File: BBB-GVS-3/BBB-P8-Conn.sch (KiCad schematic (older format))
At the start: 14 parts, among them J12 CONN_3, J13 CONN_3, J14 CONN_3, J15 CONN_3, J16 CONN_3, J17 CONN_3, J18 CONN_3, J19 CONN_3, J20 CONN_3, J21 CONN_3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

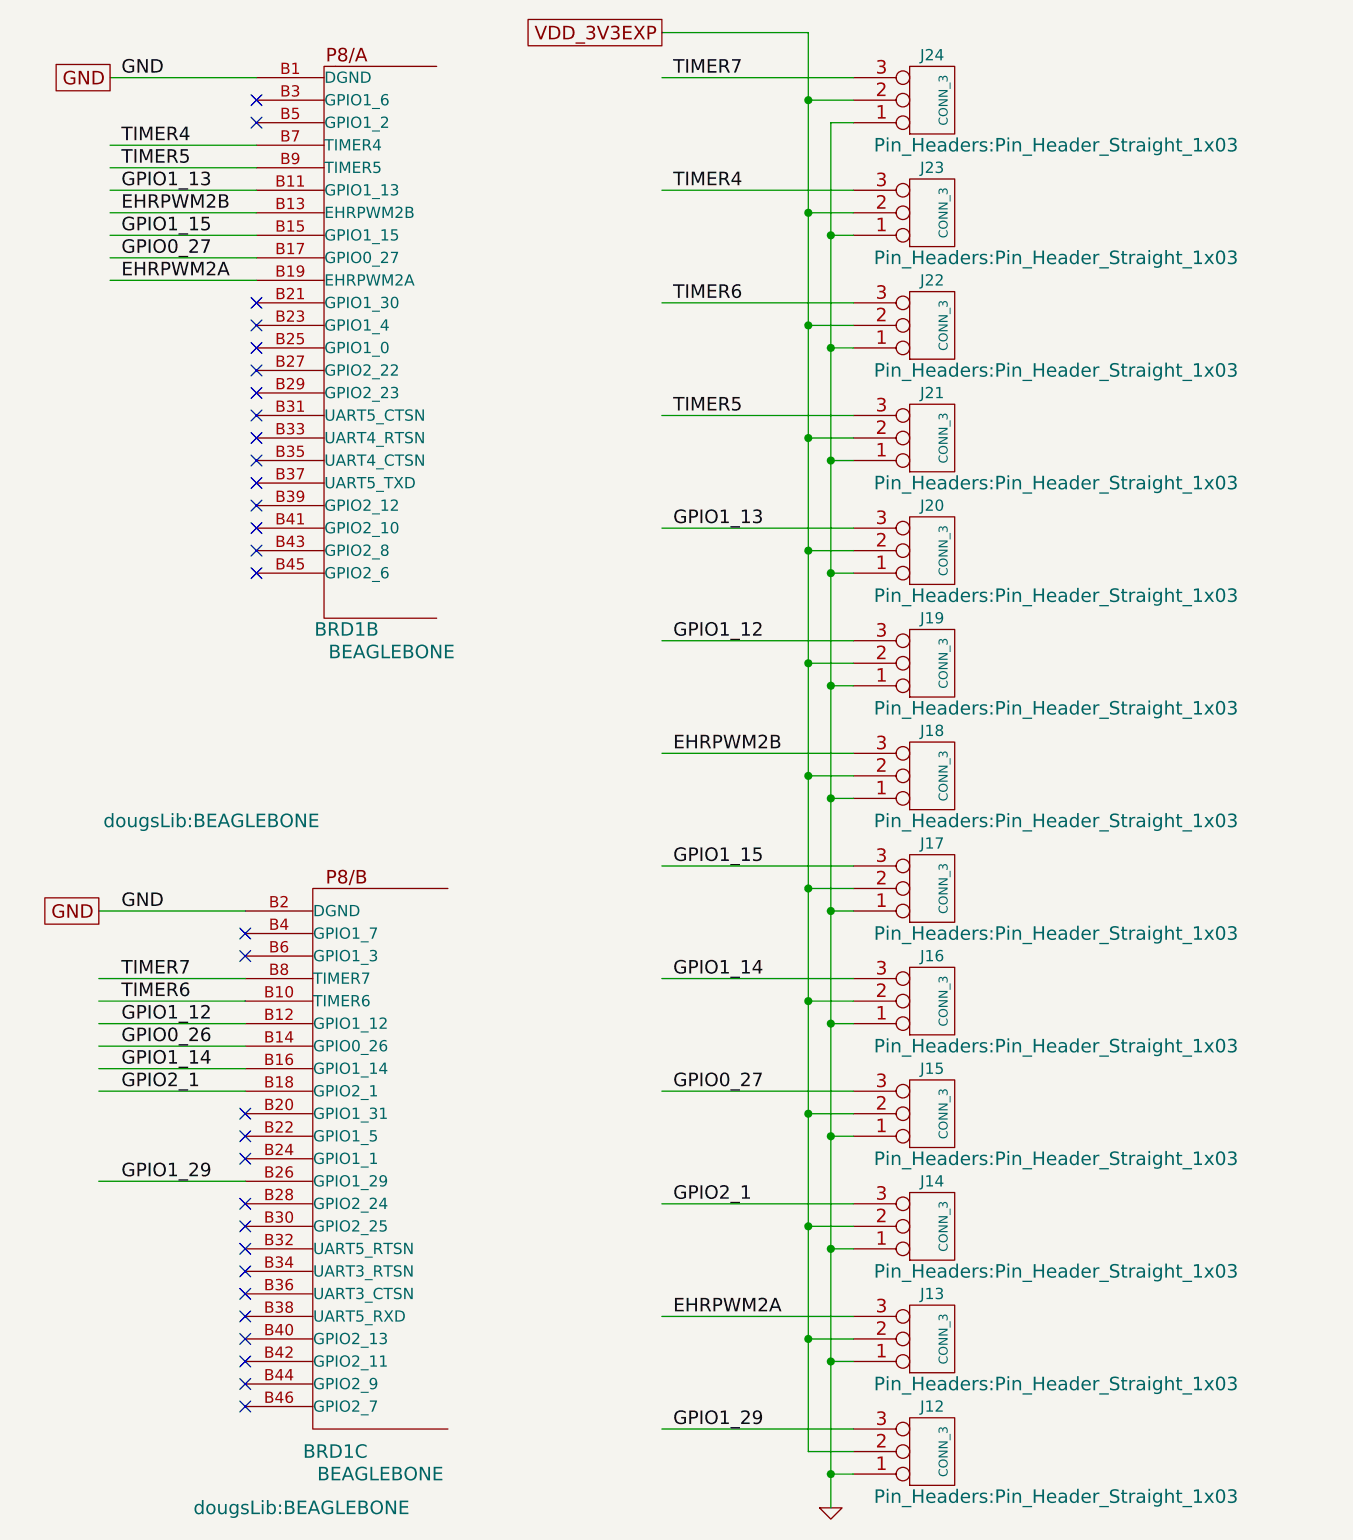
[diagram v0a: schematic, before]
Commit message: Changing GVS connector types
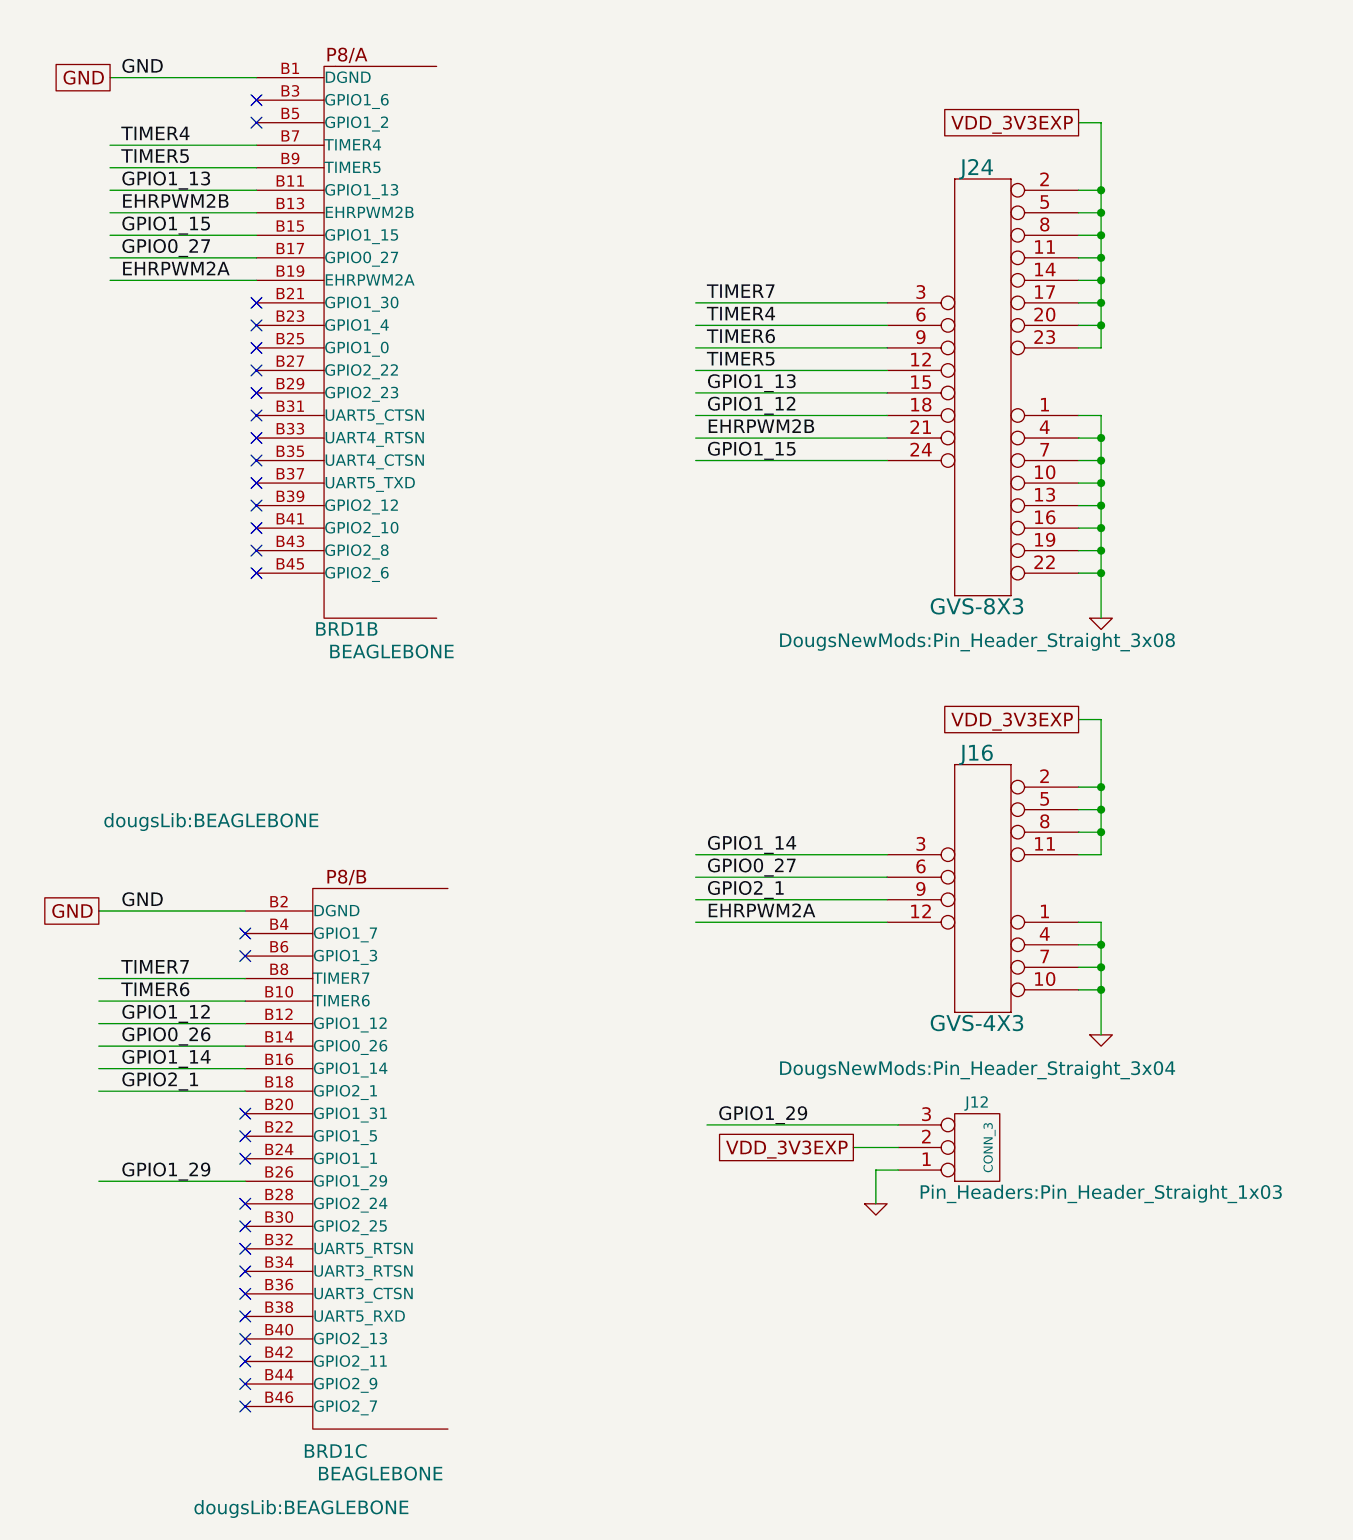
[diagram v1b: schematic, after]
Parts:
- removed J13, J14, J15, J16, J17, J18, J19, J20, J21, J22, J23, J24: CONN_3, Pin_Headers:Pin_Header_Straight_1x03, symbol CONN_3
- added J16: GVS-4X3, DougsNewMods:Pin_Header_Straight_3x04, symbol GVS-4X3
- added J24: GVS-8X3, DougsNewMods:Pin_Header_Straight_3x08, symbol GVS-8X3
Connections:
- wire segments 58 -> 62
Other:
- moved on the sheet: J12

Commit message: Changing orientation of bottom connectors
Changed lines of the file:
@@
 NoConn ~ 1600 4850
 NoConn ~ 1600 4750
-Text Label 3650 4700 0    60   ~ 0
+Text Label 3650 4400 0    60   ~ 0
 EHRPWM2A
-Text Label 3650 4500 0    60   ~ 0
+Text Label 3650 4600 0    60   ~ 0
 GPIO0_27
-Text Label 3650 2650 0    60   ~ 0
+Text Label 3700 1950 0    60   ~ 0
 GPIO1_15
-Text Label 3650 2550 0    60   ~ 0
+Text Label 3700 2050 0    60   ~ 0
 EHRPWM2B
-Text Label 3650 2350 0    60   ~ 0
+Text Label 3700 2250 0    60   ~ 0
 GPIO1_13
-Text Label 3650 2050 0    60   ~ 0
+Text Label 3700 2550 0    60   ~ 0
 TIMER4
 Wire Wire Line
@@
 Text Label 3700 5600 0    60   ~ 0
 GPIO1_29
-Text Label 3650 4600 0    60   ~ 0
+Text Label 3650 4500 0    60   ~ 0
 GPIO2_1
-Text Label 3650 4400 0    60   ~ 0
+Text Label 3650 4700 0    60   ~ 0
 GPIO1_14
-Text Label 3650 2450 0    60   ~ 0
+Text Label 3700 2150 0    60   ~ 0
 GPIO1_12
-Text Label 3650 2150 0    60   ~ 0
+Text Label 3700 2450 0    60   ~ 0
 TIMER6
-Text Label 3650 1950 0    60   ~ 0
+Text Label 3700 2650 0    60   ~ 0
 TIMER7
 Wire Wire Line
@@
 Wire Wire Line
 	1000 1350 1650 1350
-Text Label 3650 2250 0    60   ~ 0
+Text Label 3700 2350 0    60   ~ 0
 TIMER5
 Wire Wire Line
@@
 Connection ~ 5400 5000
 $Comp
-L GND #PWR?
+L GND #PWR06
 U 1 1 56883EC8
 P 5400 5200
-F 0 "#PWR?" H 5400 5200 30  0001 C CNN
+F 0 "#PWR06" H 5400 5200 30  0001 C CNN
 F 1 "GND" H 5400 5130 30  0001 C CNN
 F 2 "" H 5400 5200 60  0000 C CNN
